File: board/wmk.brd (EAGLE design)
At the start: 33.3 x 100 mm, 22 parts, among them IC1 LM1117MPX-3.3, U1 STM32F10XRXT6, X1 PN87520-S

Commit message: Dropping dependency on stm32cubeide, new makefile.
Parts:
- added JP2: (no value), pinhead:1X08
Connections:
- new net CLOCK: JP2.1, U1.11
- new net DATA: JP2.2, U1.53
- new net INUSE: JP2.8, U1.2
- new net RESET: JP2.3, U1.4
- new net STATUS: JP2.7, U1.3
- net GND: now also JP2.6
- net VCC: now also JP2.4
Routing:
- net DATA: track 0.00 -> 50.8 mm, vias 0 -> 2
- net CLOCK: track 0.00 -> 27.4 mm, vias 0 -> 1
- net RESET: track 0.00 -> 25.6 mm
- net VCC: track 104.8 -> 129.6 mm
- net STATUS: track 0.00 -> 18.2 mm
- net INUSE: track 0.00 -> 17.8 mm
- net NRST: track 32.5 -> 34.9 mm
- net GND: track 12.3 -> 13.5 mm, vias 9 -> 16
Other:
- board size 33.3 x 100 mm -> 34.5 x 100 mm
- board text added: "Clock"
- board text added: "Data"
- board text added: "Inuse"
- board text added: "Reset"
- board text added: "Ststus"
- board text removed: "kulamario@yahoo.ie"

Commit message: First pass of the CH32 proto. unchecked and untested.
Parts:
- removed C22: 4.7UF, rcl:C1206
- removed U1: STM32F10XRXT6, stm32:TQFP64
- added F1: (no value), eagle-ltspice:R1206
- added U2: STM32F103C8T6, STM32F103C8T6:QFP50P900X900X160-48N
- moved CONNECT 26.2 mm to (27.5, 82.0), turned to 0 degrees
- moved R4 25.3 mm to (27.5, 80.0), turned to 0 degrees
- moved POWER 23.3 mm to (9.94, 81.5), turned to 180 degrees
- moved R3 22.9 mm to (9.99, 79.3), turned to 180 degrees
- moved C6 11.2 mm to (22.0, 75.3), turned to 270 degrees
- moved C5 9.81 mm to (15.2, 78.3), turned to 180 degrees
- moved C10 6.23 mm to (18.3, 60.3), turned to 180 degrees
- moved C11 5.96 mm to (21.9, 60.3), turned to 0 degrees
- moved R2 5.83 mm to (25.3, 76.0), turned to 90 degrees
- moved C7 5.37 mm to (25.3, 72.1), turned to 270 degrees
- moved C16 4.85 mm to (20.3, 70.1), turned to 0 degrees
- moved C12 4.16 mm to (13.5, 71.8), turned to 90 degrees
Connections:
- net CLOCK: now also U2.16; no longer U1.11
- net DATA: now also U2.30; no longer U1.53
- net GND: now also U2.12, U2.23, U2.35, U2.44, U2.47, U2.8; no longer C22.2, U1.12, U1.16, U1.18, U1.31, U1.47, U1.60, U1.63
- net INUSE: now also U2.31; no longer U1.2
- net N$1: now also U2.5; no longer U1.5
- net N$10: now also U2.42; no longer U1.58
- net N$11: now also U2.43; no longer U1.59
- net N$13: now also U2.27; no longer U1.35
- net N$15: now also U2.26; no longer U1.34
- net N$2: now also U2.6; no longer U1.6
- net N$3: now also U2.13; no longer U1.8
- net N$36: now also U2.28; no longer U1.36
- net N$4: now also F1.2, X1.1; no longer C22.1, U1.30
- net N$6: now also U2.39; no longer U1.55
- net N$8: now also U2.40; no longer U1.56
- net N$9: now also U2.41; no longer U1.57
- net NRST: now also U2.7; no longer U1.7
- net RESET: now also U2.33; no longer U1.4
- net STATUS: now also U2.32; no longer U1.3
- net SWCLK: now also U2.37; no longer U1.49
- net SWDIO: now also U2.34; no longer U1.46
- net USB_DM: now also U2.22; no longer U1.44
- net USB_DP: now also U2.25; no longer U1.45
- net VCC: now also F1.1; no longer X1.1
- net VDD: now also U2.1, U2.24, U2.36, U2.48, U2.9; no longer U1.1, U1.13, U1.19, U1.32, U1.48, U1.64
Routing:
- net VCC: track 129.6 -> 5.09 mm, vias 0 -> 3
- net VDD: track 132.8 -> 31.1 mm, vias 8 -> 9
- net N$3: track 42.2 -> 7.37 mm, vias 2 -> 0
- net NRST: track 34.9 -> 11.7 mm, vias 3 -> 0
- net N$36: track 36.8 -> 14.9 mm
- net N$13: track 31.0 -> 9.37 mm
- net N$15: track 30.2 -> 8.62 mm
- net CLOCK: track 27.4 -> 48.2 mm, vias 1 -> 0
- net GND: track 13.5 -> 31.5 mm, vias 16 -> 12
- net DATA: track 50.8 -> 65.8 mm, vias 2 -> 0
- net SWCLK: track 21.5 -> 33.6 mm
- net INUSE: track 17.8 -> 27.9 mm
- net N$1: track 11.0 -> 21.1 mm
- net STATUS: track 18.2 -> 27.7 mm
- net RESET: track 25.6 -> 34.7 mm
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- added copper zone on layer 15, net GND
- added copper zone on layer 2, net VCC
- added copper zone on layer 2, net VDD
- removed copper zone on layer 1, net GND
- removed copper zone on layer 16, net GND

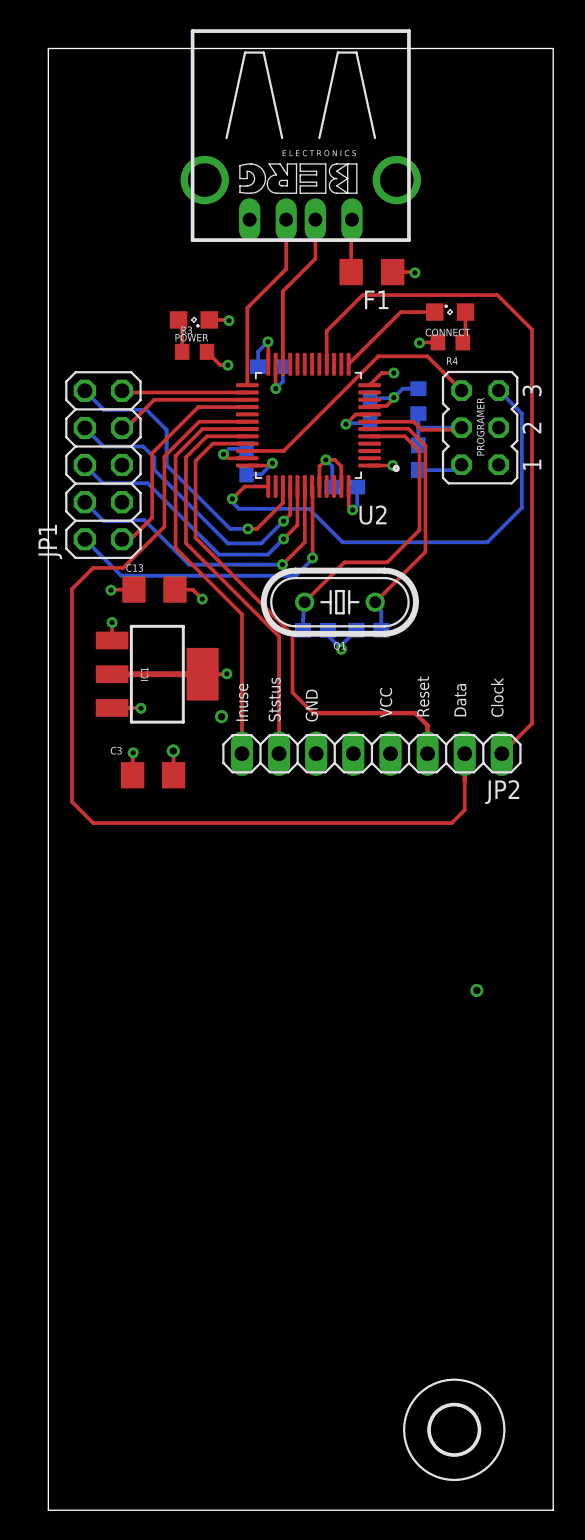
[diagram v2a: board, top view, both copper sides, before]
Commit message: Added TX/RX and moved LEDS
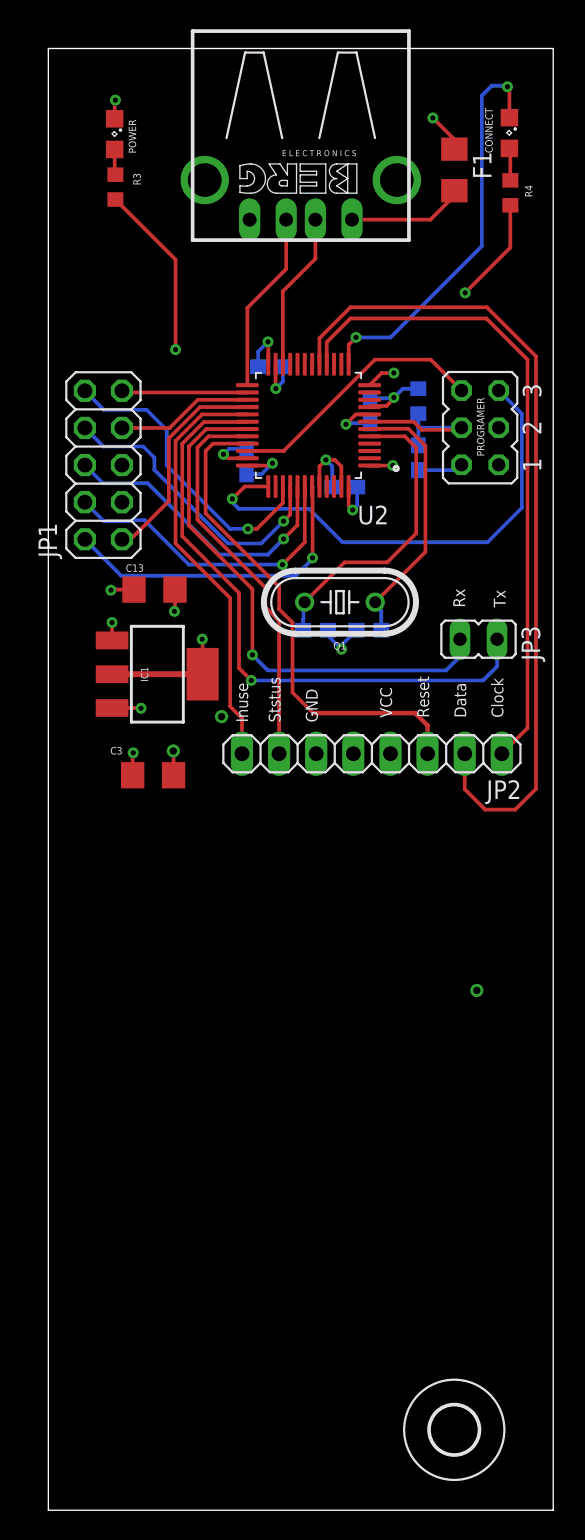
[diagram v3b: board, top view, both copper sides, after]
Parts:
- added JP3: (no value), jumper:JP1
- moved POWER 13.8 mm to (4.52, 94.2), turned to 270 degrees
- moved CONNECT 12.9 mm to (31.5, 94.3), turned to 270 degrees
- moved R3 12.5 mm to (4.57, 90.6), turned to 90 degrees
- moved R4 11.0 mm to (31.6, 90.2), turned to 90 degrees
- moved F1 8.98 mm to (27.8, 91.8), turned to 270 degrees
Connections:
- new net RX: JP3.1, U2.31
- new net TX: JP3.2, U2.30
- net DATA: now also U2.17; no longer U2.30
- net INUSE: now also U2.29; no longer U2.31
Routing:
- net TX: track 0.00 -> 42.3 mm, vias 0 -> 1
- net RX: track 0.00 -> 36.8 mm, vias 0 -> 1
- net N$3: track 7.37 -> 27.8 mm, vias 0 -> 2
- net VDD: track 31.1 -> 47.3 mm
- net DATA: track 65.8 -> 56.9 mm
- net N$4: track 3.61 -> 8.02 mm
- net CLOCK: track 48.2 -> 44.8 mm
- net VCC: track 5.09 -> 6.28 mm
- net INUSE: track 27.9 -> 28.9 mm
- net STATUS: track 27.7 -> 27.0 mm
- net RESET: track 34.7 -> 34.2 mm
- net N$12: track 2.28 -> 1.74 mm
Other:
- board text added: "Rx"
- board text added: "Tx"
